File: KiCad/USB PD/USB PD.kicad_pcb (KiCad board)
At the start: 2 copper layers, 40 x 50 mm, 34 parts, among them J1 ESP32 Jumpers, J10 Conn_01x02_Pin, J11 Conn_01x02_Pin, J12 Conn_01x03_Pin, J13 Conn_01x02_Pin, J2 Conn_01x02_Pin, J9 Conn_01x02_Pin, U1 AO3400A, U2 IP2721, U3 TPS5430DDAR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

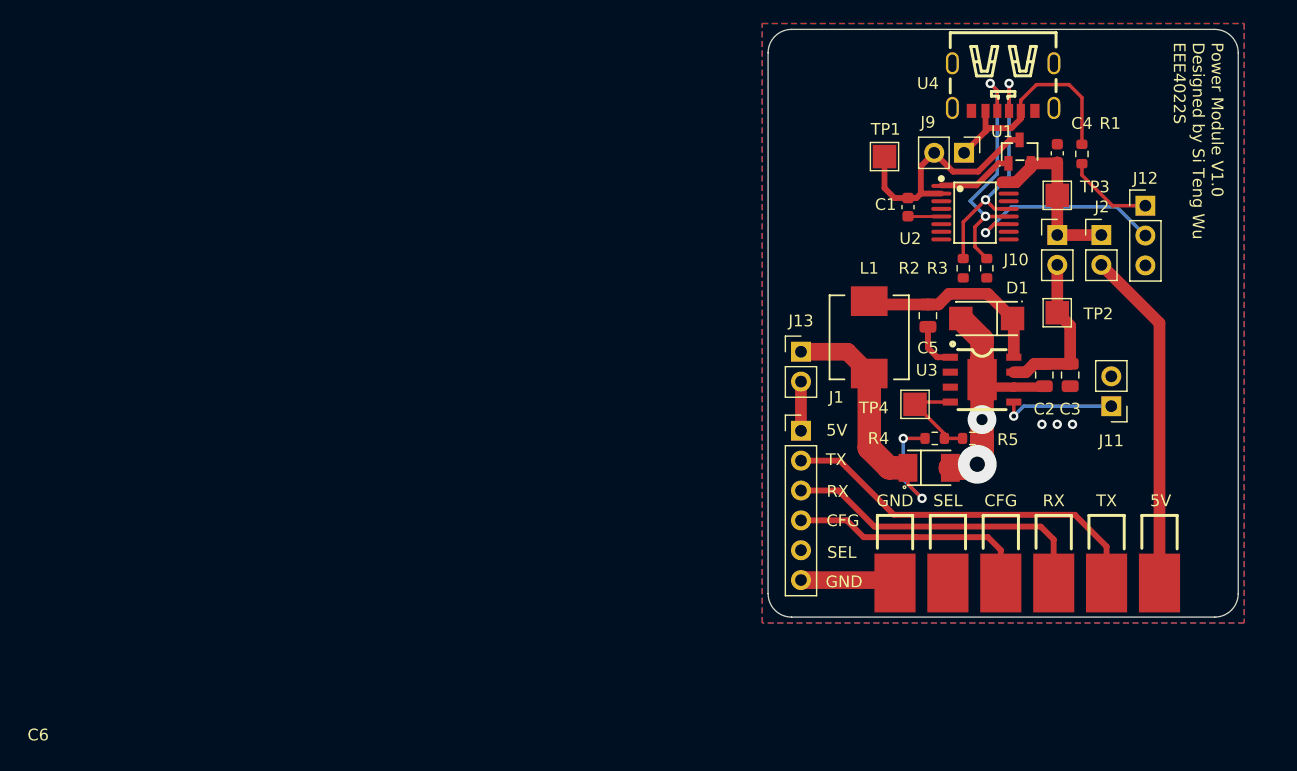
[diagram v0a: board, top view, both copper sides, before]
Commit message: Updated USB PD and Driver LED circuit
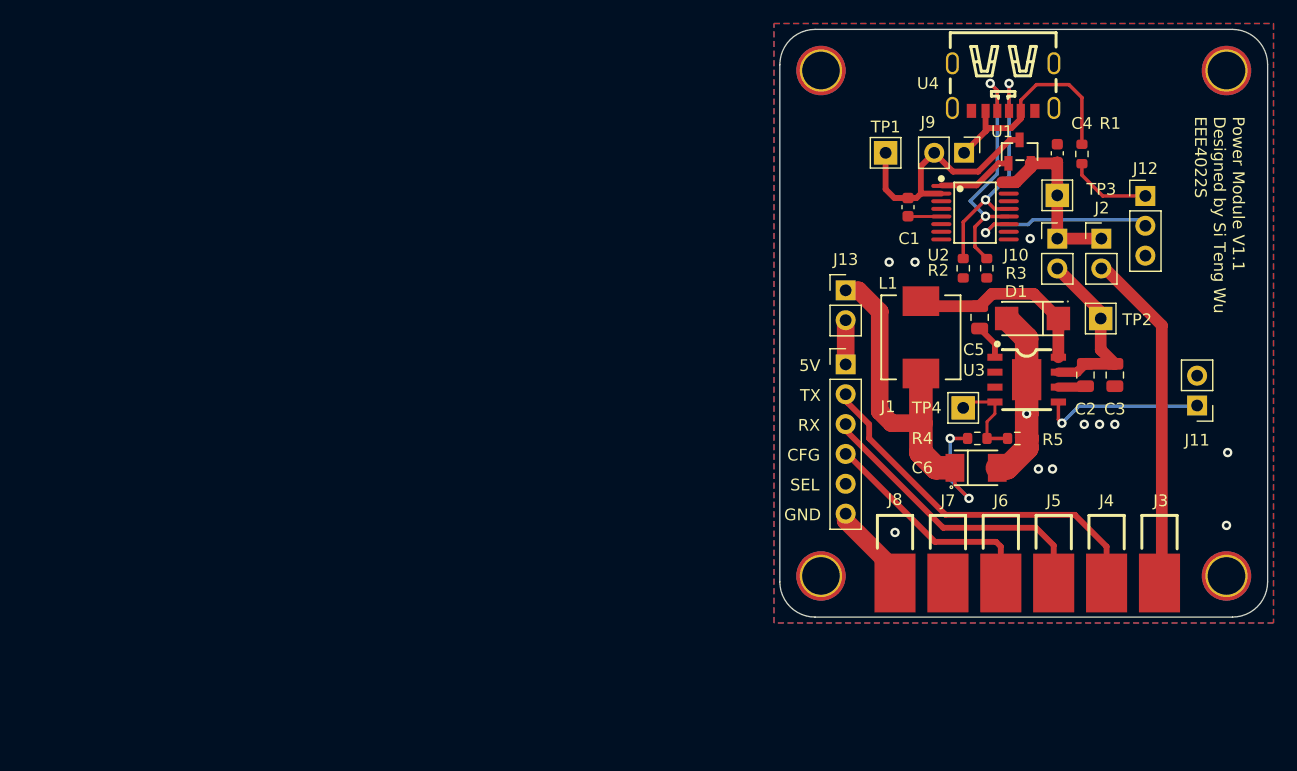
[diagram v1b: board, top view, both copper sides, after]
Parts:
- added H1: M3, Library:MountingHole_3.2mm_M3_Pad_TopBottom, F.Cu at (134.5, 78.5)
- added H2: M3, Library:MountingHole_3.2mm_M3_Pad_TopBottom, F.Cu at (169.0, 78.5)
- added H3: M3, Library:MountingHole_3.2mm_M3_Pad_TopBottom, F.Cu at (134.5, 121.5)
- added H4: M3, Library:MountingHole_3.2mm_M3_Pad_TopBottom, F.Cu at (169.0, 121.5)
- L1: value 22uF -> 22uH
- TP1, TP2, TP3, TP4: footprint TestPoint:TestPoint_Pad_2.0x2.0mm -> Library:TestPoint_THTPad_2.0x2.0mm_Drill1.0mm
- moved J11 7.30 mm to (166.5, 107.0)
- moved J1 6.81 mm to (136.6, 103.5)
- moved J13 6.46 mm to (136.6, 97.2)
- moved C5 4.40 mm to (148.0, 99.5)
- moved L1 4.39 mm to (143.0, 101.2)
- moved TP4 4.11 mm to (146.6, 107.2)
- moved C6 3.99 mm to (147.7, 112.3)
- moved D1 3.90 mm to (152.5, 99.6)
- moved R5 3.83 mm to (151.2, 109.8)
- moved C3 3.80 mm to (159.5, 104.4)
- moved U3 3.79 mm to (152.0, 104.8)
- moved TP2 3.73 mm to (158.3, 99.6)
- moved R4 3.62 mm to (147.8, 109.8)
- moved C2 3.50 mm to (157.0, 104.4)
- moved J12 0.83 mm to (162.1, 89.2)
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- renumbered 5V to J3, TX to J4, RX to J5, CFG to J6, SEL to J7, GND to J8
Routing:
- net GND: track 38.3 -> 28.1 mm, vias 5 -> 12
- net Net-(J11-Pin_1): track 9.85 -> 14.0 mm
- net Net-(J13-Pin_1): track 33.3 -> 35.8 mm
- net Net-(J1-Pin_3): track 26.9 -> 25.5 mm
- net Net-(J1-Pin_4): track 20.8 -> 19.6 mm
- net Net-(J10-Pin_2): track 14.0 -> 15.2 mm
- net Net-(J12-Pin_2): track 17.8 -> 16.5 mm
- net Net-(U3-BOOT): track 4.03 -> 2.98 mm
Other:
- board size 40 x 50 mm -> 41.5 x 50 mm
- board text added: "Power Module V1.1 Designed by Si Teng Wu EEE4022S"
- board text removed: "Power Module V1.0 Designed by Si Teng Wu EEE4022S"
